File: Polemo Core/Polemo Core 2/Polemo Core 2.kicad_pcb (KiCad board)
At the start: 4 copper layers, 40 x 100 mm, 174 parts, among them P1 Header-Male-2.54_2x2, P2 Header-Male-2.54_2x2, Q1 BC847_C2910145, Q2 MMBT5551LT1G, Q3 AO3401A, Q4 AO3401A, Q5 MMBT5551LT1G, U1 ATSAML21G18B-AUT, U10 74LVC1G08GV,125, U11 LT3014BHVES5#TRMPBF, U12 TXU0202DCUR, U13 TLV7031DBVR, U14 TLR341G-GTR, U15 803-87-006-10-001101, U2 XC6209F332MR-G, U3 MC14043BDR2G, U4 LMV793MFX/NOPB, U5 TPS7A2030PDBVR, U6 TLV3201AIDBVT, U7 OPA357AIDBVR, U8 TLR341G-GTR, U9 MF-ASML020/6-2, X1 32.768kHz

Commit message: Added V1.2 files
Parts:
- moved X1 22.0 mm to (60.2, 108.4), turned to 135 degrees
- moved C43 18.6 mm to (61.1, 105.0), turned to -45 degrees
- moved C42 16.3 mm to (64.0, 107.7), turned to 135 degrees
- moved U11 6.70 mm to (68.3, 112.4)
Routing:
- net GND: track 60.6 -> 0.00 mm, vias 2 -> 0
- net Vload: track 0.00 -> 30.5 mm
- net Net-(U1-PA01): track 0.00 -> 9.59 mm
- net Net-(U1-PA00): track 0.00 -> 9.09 mm
- net USBDP: track 3.05 -> 0.00 mm
- added copper zone on B.Cu, net GND
- added copper zone on F.Cu, net GND
- added copper zone on In1.Cu, net GND

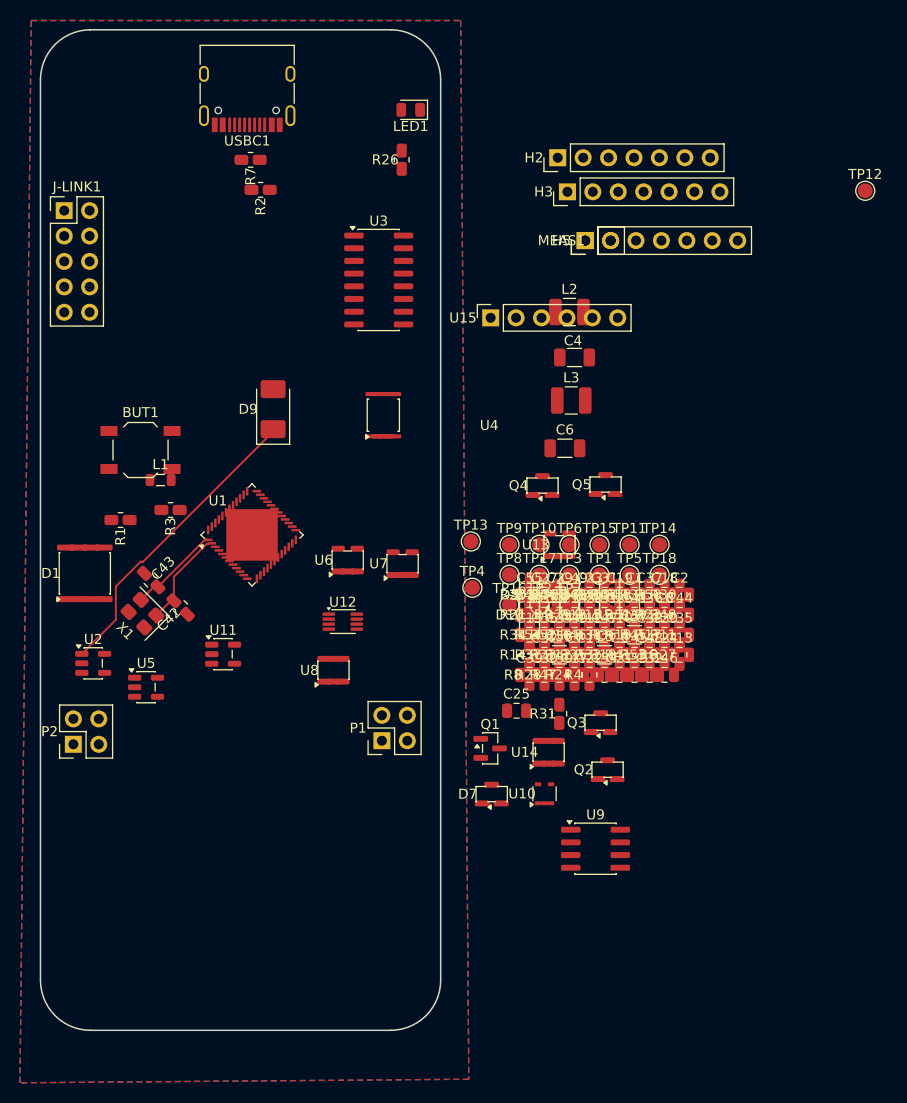
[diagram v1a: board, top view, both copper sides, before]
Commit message: Moved more components around
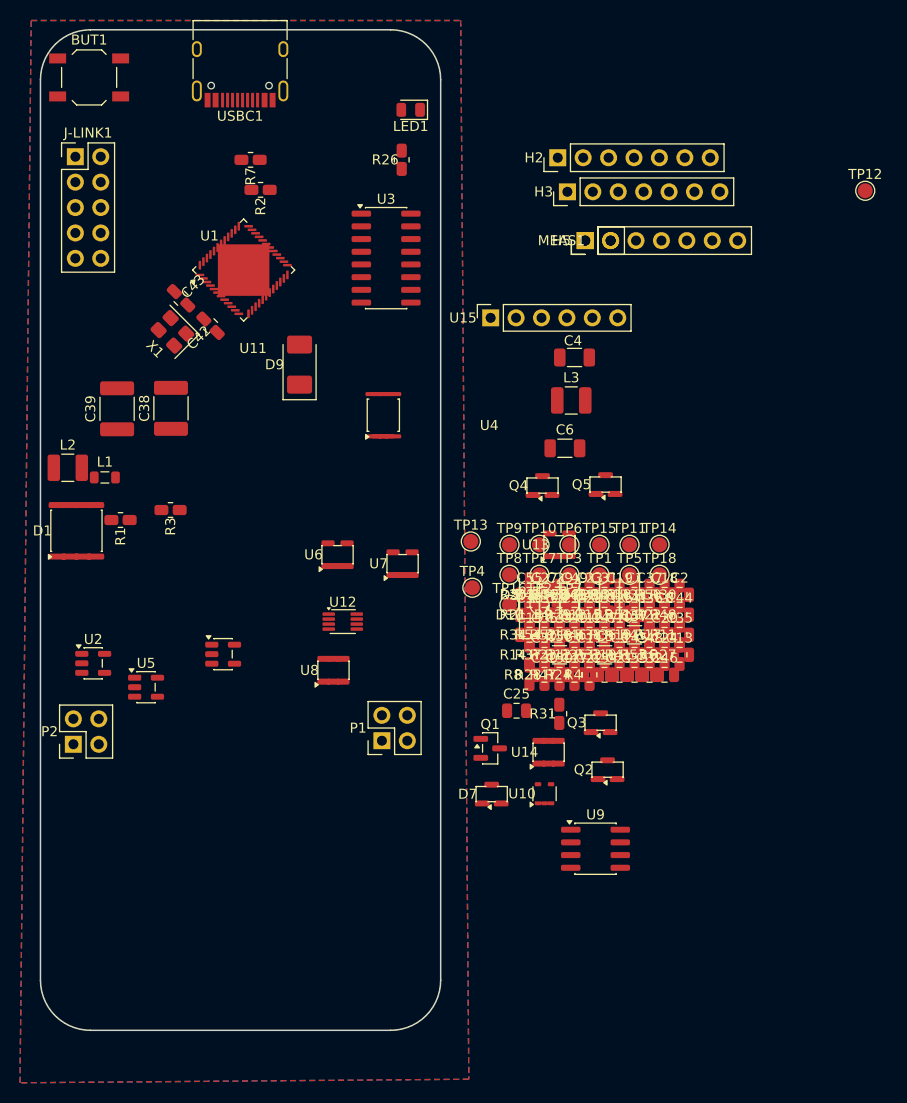
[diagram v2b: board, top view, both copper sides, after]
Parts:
- C38, C39: footprint Capacitor_SMD:C_0805_2012Metric -> Capacitor_SMD:C_1812_4532Metric
- moved C38 52.9 mm to (63.0, 87.8), turned to 90 degrees
- moved L2 52.5 mm to (52.7, 93.8)
- moved C39 49.0 mm to (57.7, 87.9), turned to 90 degrees
- moved BUT1 37.6 mm to (54.9, 54.8)
- moved C43 28.3 mm to (64.1, 76.8)
- moved C42 28.3 mm to (67.0, 79.6)
- moved X1 28.3 mm to (63.2, 80.2)
- moved U1 26.5 mm to (70.3, 74.0)
- moved L1 5.57 mm to (56.4, 94.7)
- moved J-LINK1 5.50 mm to (53.5, 62.7)
- moved D9 5.18 mm to (75.9, 83.5)
- moved D1 4.33 mm to (53.6, 100.1)
- moved USBC1 2.57 mm to (70.0, 53.0)
- moved U3 2.31 mm to (84.5, 72.8)
- moved U6 1.15 mm to (79.7, 102.5)
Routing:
- net Vload: track 30.5 -> 0.00 mm
- net Net-(U1-PA01): track 9.59 -> 0.00 mm
- net Net-(U1-PA00): track 9.09 -> 0.00 mm
